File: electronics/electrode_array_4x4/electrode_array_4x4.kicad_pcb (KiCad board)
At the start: 2 copper layers, 2 parts

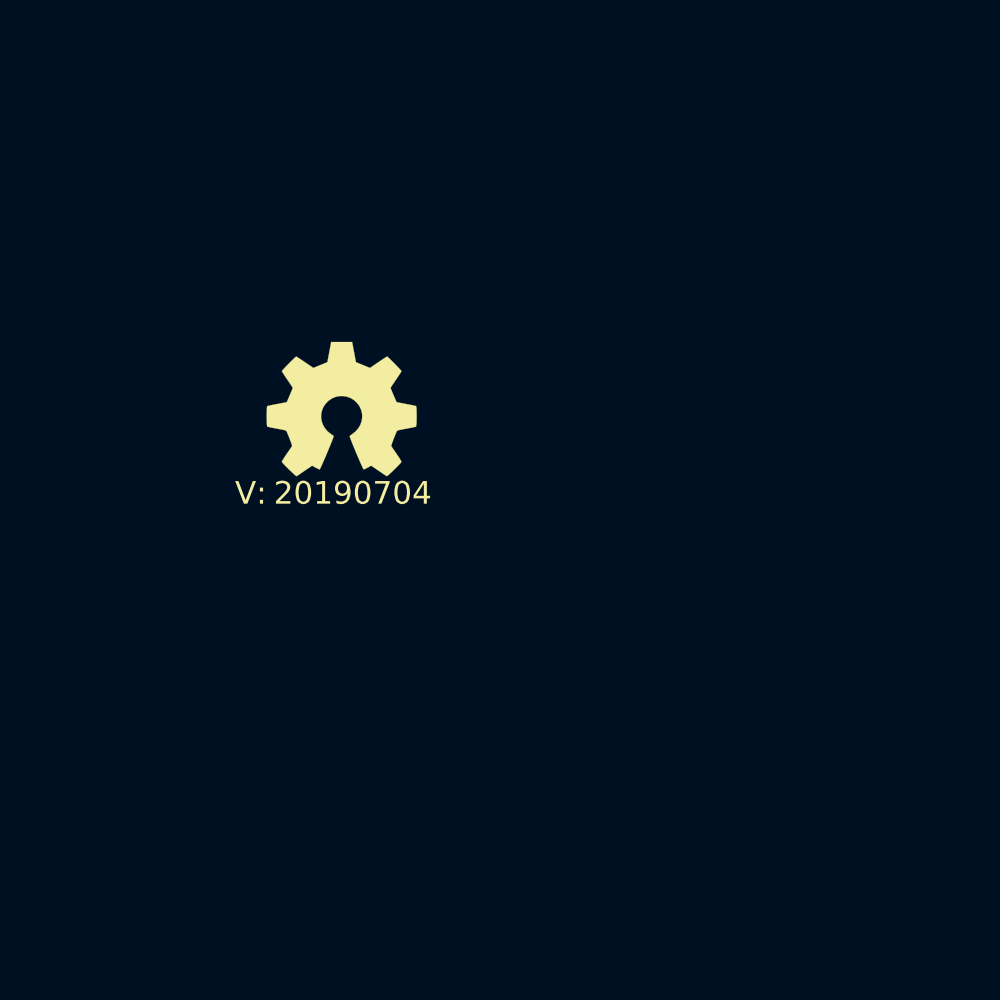
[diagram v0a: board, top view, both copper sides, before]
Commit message: completed 4by4 electrode array
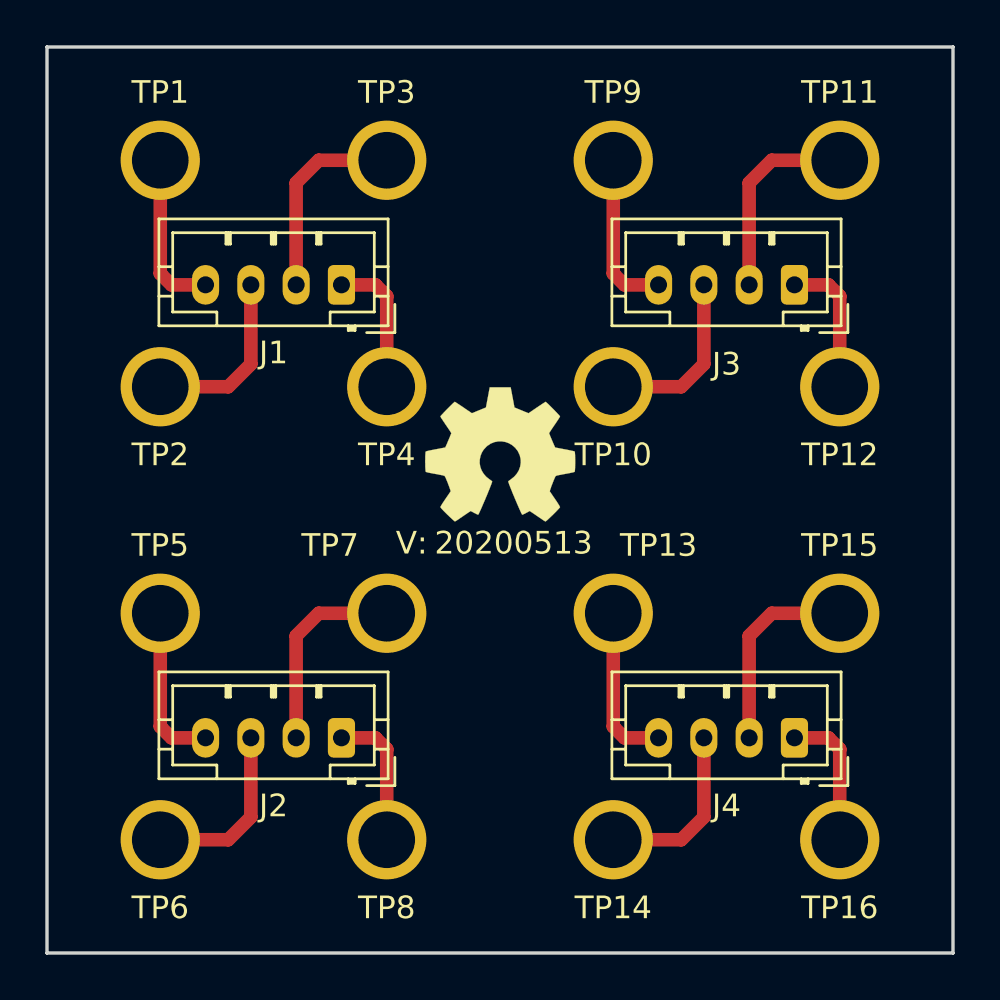
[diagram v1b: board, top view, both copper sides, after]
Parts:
- added J1: Conn_01x04, Connector_JST:JST_PH_B4B-PH-K_1x04_P2.00mm_Vertical, F.Cu at (148.0, 95.5)
- added J2: Conn_01x04, Connector_JST:JST_PH_B4B-PH-K_1x04_P2.00mm_Vertical, F.Cu at (148.0, 115.5)
- added J3: Conn_01x04, Connector_JST:JST_PH_B4B-PH-K_1x04_P2.00mm_Vertical, F.Cu at (168.0, 95.5)
- added J4: Conn_01x04, Connector_JST:JST_PH_B4B-PH-K_1x04_P2.00mm_Vertical, F.Cu at (168.0, 115.5)
- added TP1: testpad, SquantorSpecial:hugepad_35X25hole, F.Cu at (140.0, 90.0)
- added TP10: testpad, SquantorSpecial:hugepad_35X25hole, F.Cu at (160.0, 100.0)
- added TP11: testpad, SquantorSpecial:hugepad_35X25hole, F.Cu at (170.0, 90.0)
- added TP12: testpad, SquantorSpecial:hugepad_35X25hole, F.Cu at (170.0, 100.0)
- added TP13: testpad, SquantorSpecial:hugepad_35X25hole, F.Cu at (160.0, 110.0)
- added TP14: testpad, SquantorSpecial:hugepad_35X25hole, F.Cu at (160.0, 120.0)
- added TP15: testpad, SquantorSpecial:hugepad_35X25hole, F.Cu at (170.0, 110.0)
- added TP16: testpad, SquantorSpecial:hugepad_35X25hole, F.Cu at (170.0, 120.0)
- added TP2: testpad, SquantorSpecial:hugepad_35X25hole, F.Cu at (140.0, 100.0)
- added TP3: testpad, SquantorSpecial:hugepad_35X25hole, F.Cu at (150.0, 90.0)
- added TP4: testpad, SquantorSpecial:hugepad_35X25hole, F.Cu at (150.0, 100.0)
- added TP5: testpad, SquantorSpecial:hugepad_35X25hole, F.Cu at (140.0, 110.0)
- added TP6: testpad, SquantorSpecial:hugepad_35X25hole, F.Cu at (140.0, 120.0)
- added TP7: testpad, SquantorSpecial:hugepad_35X25hole, F.Cu at (150.0, 110.0)
- added TP8: testpad, SquantorSpecial:hugepad_35X25hole, F.Cu at (150.0, 120.0)
- added TP9: testpad, SquantorSpecial:hugepad_35X25hole, F.Cu at (160.0, 90.0)
- N1: footprint Symbols:OSHW-Symbol_6.7x6mm_SilkScreen -> Symbol:OSHW-Symbol_6.7x6mm_SilkScreen
- N2: value 20190704 -> 20200513
- moved N2 7.43 mm to (156.0, 107.0)
- moved N1 7.28 mm to (155.0, 103.0)
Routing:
- net /C4: track 0.00 -> 8.91 mm
- net /C2: track 0.00 -> 8.91 mm
- net /A4: track 0.00 -> 8.91 mm
- net /A2: track 0.00 -> 8.91 mm
- net /D3: track 0.00 -> 7.91 mm
- net /D1: track 0.00 -> 7.91 mm
- net /B3: track 0.00 -> 7.91 mm
- net /B1: track 0.00 -> 7.91 mm
- net /C3: track 0.00 -> 7.21 mm
- net /C1: track 0.00 -> 7.21 mm
- net /A3: track 0.00 -> 7.21 mm
- net /A1: track 0.00 -> 7.21 mm
- net /D4: track 0.00 -> 6.21 mm
- net /D2: track 0.00 -> 6.21 mm
- net /B4: track 0.00 -> 6.21 mm
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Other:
- board outline added: 40 x 40 mm
